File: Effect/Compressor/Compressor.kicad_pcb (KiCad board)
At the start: 2 copper layers, 30 x 62 mm, 40 parts, among them J1 Conn_01x04_Pin, J2 Conn_01x04_Pin, Q1 DMMT5551, Q2 MMBF5103, Q3 DMMT5551, Q4 MMBF5103

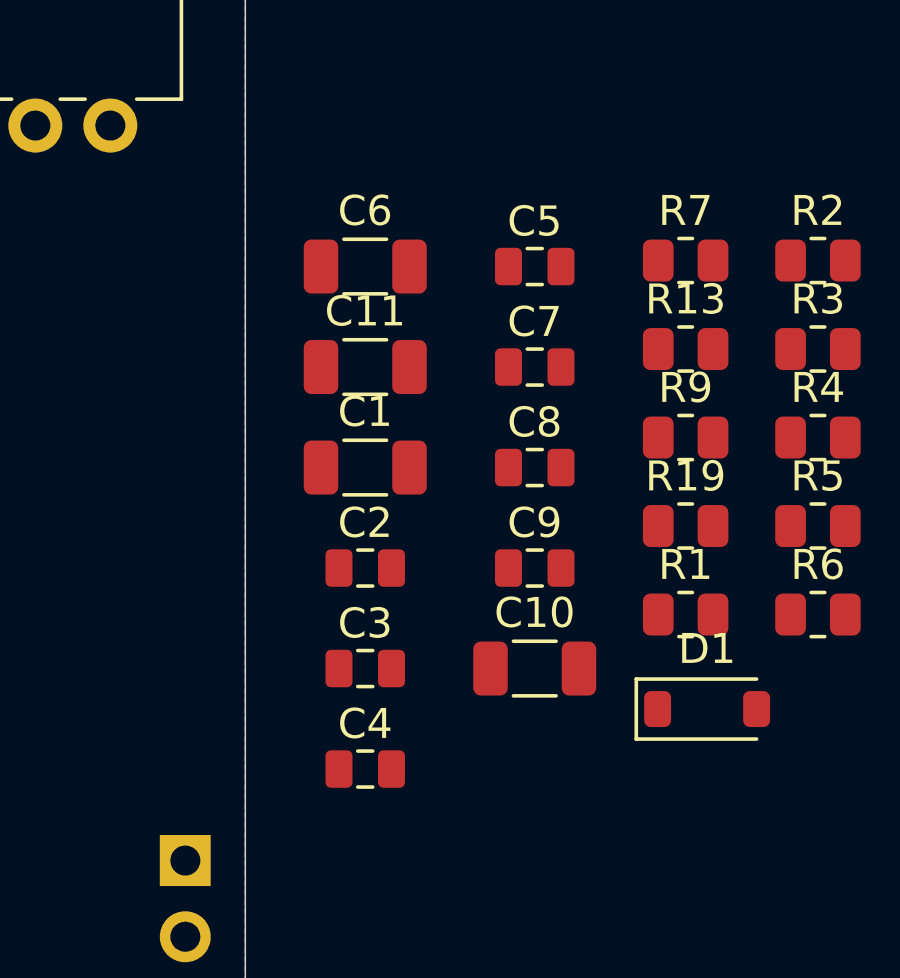
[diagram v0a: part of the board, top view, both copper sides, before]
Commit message: Compressor: Use bigger capacitors in signal path
This just changes the 0.1uF caps in the signal path to 0.47uF ones.
That doesn't fix all ills, but it should pass lower frequency signals a
bit better.

This does make them 1206 footprints, and maybe the board will be a bit
tight.  I'm starting to look at the PCB next.

Signed-off-by: Linus Torvalds <torvalds@linux-foundation.org>
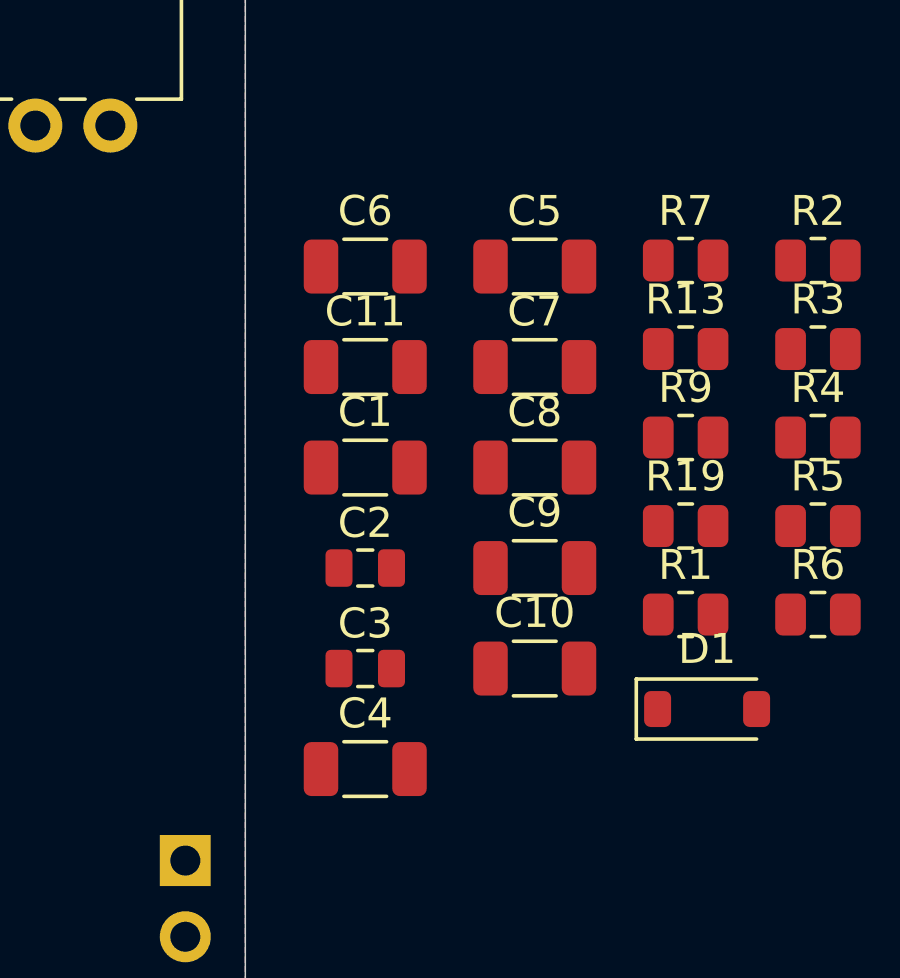
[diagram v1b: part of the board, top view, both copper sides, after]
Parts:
- C4, C5, C7, C8, C9: value 0.1uF -> 0.47uF; footprint Mylib:C_0704_1810Metric -> Capacitor_SMD:C_1206_3216Metric

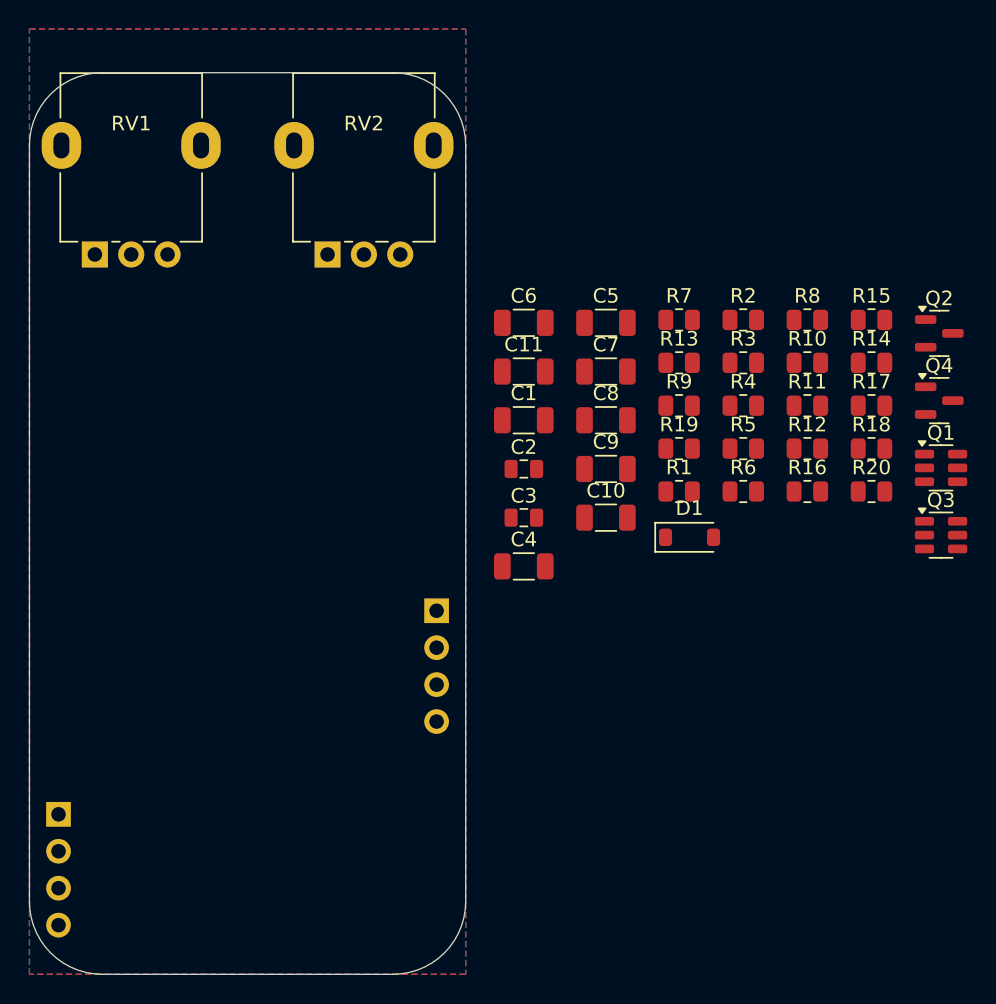
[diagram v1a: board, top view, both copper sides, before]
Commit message: Compressor: do a first PCB layout
I thought this was going to be tighter than it was, so I started laying
out things unnecessarily densely.  Also, the lower left section (the
final signal amplification) would actually have been better off moved up
closer to the volume pot, but by the time I realized that I had tons of
space and shouldn't have squeezed things down there, it was mostly done
and I just didn't bother to change it to make a nicer layout.

I just want to know if this works at all, or if the simulation is just
being unreasonably optimistic.

If it actually works, I'll at a minimum want some kind of "it's now
starting to compress" LED or similar.  And I'd want to do it as a
feedback loop rather than as based purely on input volume (I did
actually simulate a first version of that and it looked doable, but
decided that I really want to get this one done and tested before taking
that step).

Put another way: if this is even remotely usable, I'll make bigger
changes that would result in a complete re-layout anyway, so no point in
worrying over-much about this not being a particularly nice layout.

Signed-off-by: Linus Torvalds <torvalds@linux-foundation.org>
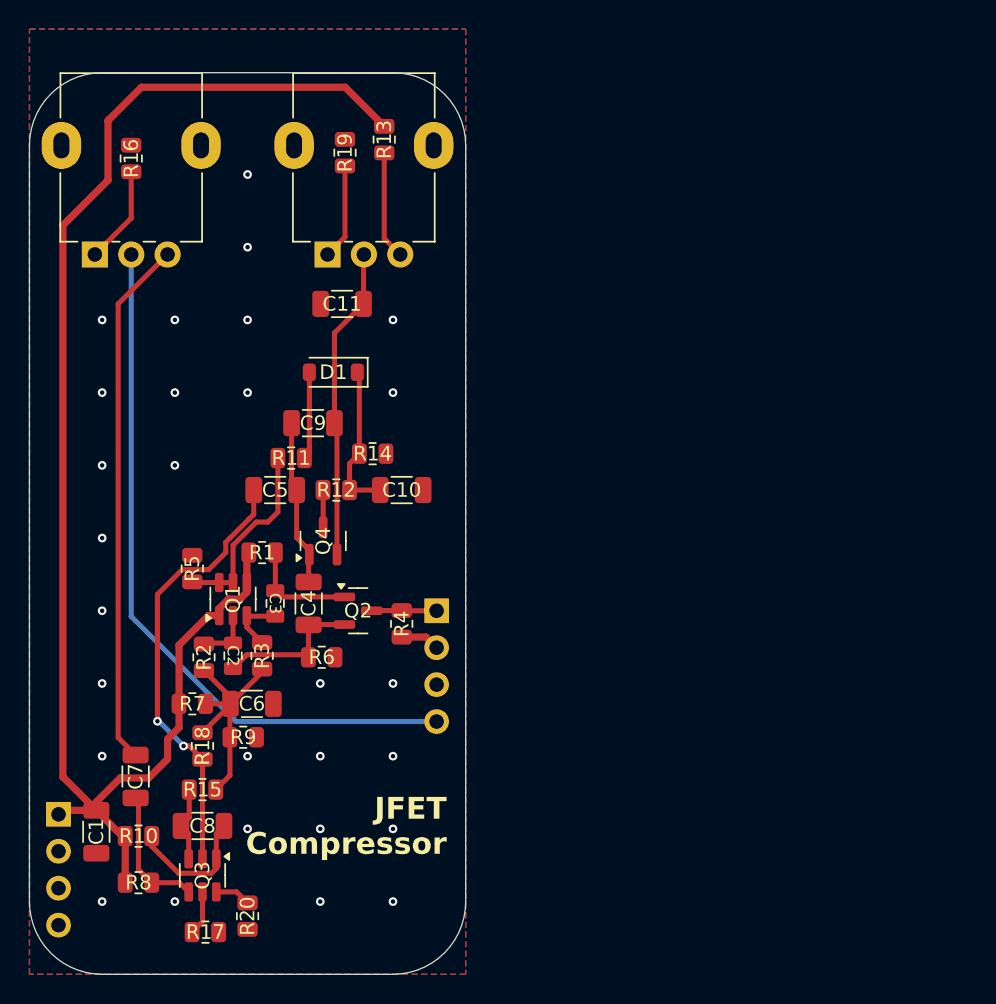
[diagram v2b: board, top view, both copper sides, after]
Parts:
- moved R8 60.1 mm to (92.5, 118.7)
- moved R17 58.4 mm to (97.1, 122.1)
- moved R10 56.3 mm to (92.5, 115.5)
- moved R15 56.2 mm to (96.9, 112.3)
- moved Q3 55.9 mm to (96.9, 118.2), turned to -90 degrees
- moved R20 51.9 mm to (100.0, 121.0), turned to -90 degrees
- moved R16 51.8 mm to (92.0, 68.9), turned to 90 degrees
- moved R18 50.3 mm to (96.9, 109.3), turned to 90 degrees
- moved Q1 49.5 mm to (99.0, 99.2), turned to 90 degrees
- moved Q2 44.3 mm to (107.6, 100.0)
- moved R2 43.7 mm to (97.0, 103.2), turned to -90 degrees
- moved Q4 43.5 mm to (105.2, 95.2), turned to 90 degrees
- moved C7 42.7 mm to (92.3, 111.4), turned to -90 degrees
- moved R7 42.6 mm to (96.2, 106.4)
- moved C1 40.8 mm to (89.6, 115.2), turned to -90 degrees
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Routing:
- net +V: track 0.00 -> 103.5 mm
- net OUT: track 0.00 -> 48.9 mm
- net Net-(C7-Pad1): track 0.00 -> 36.3 mm
- net COMPRESSED: track 0.00 -> 30.7 mm, vias 0 -> 2
- net JFETBIAS: track 0.00 -> 21.5 mm
- net VBIAS: track 0.00 -> 17.1 mm
- net RECT: track 0.00 -> 13.1 mm
- net Net-(Q4-D): track 0.00 -> 11.5 mm
- net Net-(D1-K): track 0.00 -> 10.5 mm
- net BUF: track 0.00 -> 10.4 mm
- net Net-(Q3A-C): track 0.00 -> 9.18 mm
- net Net-(Q3B-C): track 0.00 -> 9.09 mm
- net BUF_NOT: track 0.00 -> 7.57 mm
- net Net-(R13-Pad2): track 0.00 -> 7.44 mm
- net Net-(R16-Pad1): track 0.00 -> 6.72 mm
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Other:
- board text added: "JFET Compressor"

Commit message: Compressor: do PCB layout for the new design
As expected, this was much easier due to the simpler schematic for the
much more straightforward design.

Signed-off-by: Linus Torvalds <torvalds@linux-foundation.org>
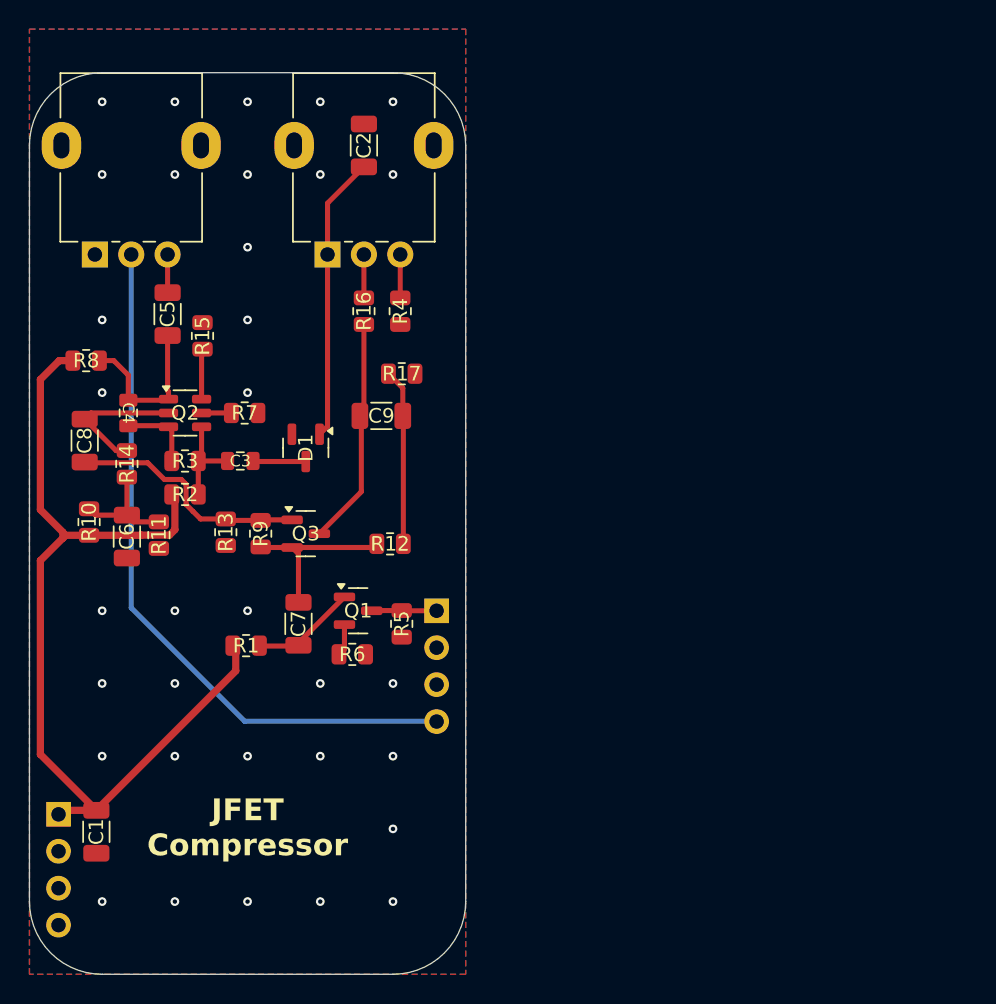
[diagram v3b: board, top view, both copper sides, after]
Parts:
- removed C10: 10uF, Capacitor_SMD:C_1206_3216Metric
- removed C11: 22uF, Capacitor_SMD:C_1206_3216Metric
- removed the Q1 at (99.0, 99.2)
- removed Q4: MMBF5103, Package_TO_SOT_SMD:SOT-23
- removed R18, R19: 100k, Resistor_SMD:R_0805_2012Metric
- removed R20: 3k3, Resistor_SMD:R_0805_2012Metric
- removed the R5 at (96.2, 97.1)
- added Q2: DMMT5551, Package_TO_SOT_SMD:SOT-23-6, F.Cu at (95.7, 86.4)
- added R4: 47k, Resistor_SMD:R_0805_2012Metric, F.Cu at (110.5, 79.4)
- C2: value 0.1uF -> 1uF; footprint Mylib:C_0704_1810Metric -> Capacitor_SMD:C_1206_3216Metric
- C4: value 0.47uF -> 0.1uF; footprint Capacitor_SMD:C_1206_3216Metric -> Mylib:C_0704_1810Metric
- C5, C7, C8: value 0.47uF -> 1uF
- C9: value 0.47uF -> 22nF
- D1: value BAT41Z -> BAT54S-SOT-23-3; footprint Diode_SMD:D_SOD-123 -> Package_TO_SOT_SMD:SOT-23
- Q3: value DMMT5551 -> MMBF5103; footprint Package_TO_SOT_SMD:SOT-23-6 -> Package_TO_SOT_SMD:SOT-23
- R1: value 1k -> 1k5
- R10: value 10k -> 100k
- R11: value 1k -> 33k
- R13: value 160k -> 4k7
- R14: value 1MEG -> 100k
- R15, R7: value 100k -> 3k3
- R16: value 22k -> 1MEG
- R17: value 3k3 -> 100k
- R2: value 100k -> 10k
- R3: value 100k -> 560k
- moved R17 40.7 mm to (110.6, 83.7)
- moved C2 36.2 mm to (108.0, 68.0), turned to 90 degrees
- moved R8 36.1 mm to (88.9, 82.8)
- moved R15 31.2 mm to (96.9, 81.1), turned to 90 degrees
- moved R13 29.1 mm to (98.5, 94.6)
- moved C8 27.7 mm to (88.8, 88.3), turned to 90 degrees
- moved Q3 24.5 mm to (104.0, 94.7), turned to 0 degrees
- moved R10 21.9 mm to (89.1, 93.9), turned to -90 degrees
- moved R7 20.3 mm to (99.8, 86.4)
- moved R16 19.1 mm to (108.0, 79.4), turned to -90 degrees
- moved C4 18.0 mm to (91.8, 86.4)
- moved R14 16.9 mm to (91.7, 89.9), turned to 90 degrees
- moved RV1 16.0 mm to (108.0, 68.0)
- moved RV2 16.0 mm to (92.0, 68.0)
- moved C7 15.4 mm to (103.5, 100.9), turned to 90 degrees
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- renumbered Q2 to Q1, R4 to R5
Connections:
- C2 pad 1: Net-(Q1A-B) -> RECT
- C2 pad 2: BUF -> GND
- C3 pad 1: BUF_NOT -> Net-(Q2B-C)
- C3 pad 2: Net-(Q1B-B) -> Net-(D1-COM)
- C4 pad 1: Net-(Q4-D) -> FB
- C4 pad 2: BUF -> Net-(Q2B-B)
- C5 pad 1: COMPRESSED -> FB
- C5 pad 2: Net-(Q4-D) -> Net-(C5-Pad2)
- C7 pad 1: Net-(C7-Pad1) -> BUF_IN
- C7 pad 2: Net-(Q3B-C) -> Net-(Q3-S)
- C8 pad 1: Net-(Q3B-B) -> Net-(Q3-D)
- C8 pad 2: Net-(Q3A-C) -> Net-(Q2A-B)
- C9 pad 1: Net-(Q4-D) -> Net-(C9-Pad1)
- C9 pad 2: JFETBIAS -> Net-(Q3-G)
- D1 pad 1: Net-(D1-K) -> RECT
- D1 pad 2: Net-(D1-A) -> GND
- Q1 pad 1: BUF_NOT -> BUF_IN
- Q1 pad 2: BUF -> Net-(Q1-S)
- Q3 pad 1: Net-(Q3A-C) -> Net-(Q3-D)
- Q3 pad 2: COMPRESSED -> Net-(Q3-S)
- Q3 pad 3: Net-(Q3B-B) -> Net-(Q3-G)
- R1 pad 2: BUF_NOT -> BUF_IN
- R10 pad 1: +V -> VBIAS
- R10 pad 2: Net-(Q3A-C) -> +V
- R11 pad 1: Net-(D1-A) -> GND
- R11 pad 2: RECT -> VBIAS
- R12 pad 1: CONTROL -> Net-(Q3-S)
- R12 pad 2: Net-(D1-K) -> Net-(C9-Pad1)
- R13 pad 1: +V -> Net-(Q3-D)
- R13 pad 2: Net-(R13-Pad2) -> GND
- R14 pad 1: GND -> VBIAS
- R14 pad 2: Net-(D1-K) -> Net-(Q2A-B)
- R15 pad 1: Net-(Q3B-B) -> Net-(Q2A-E)
- R15 pad 2: VBIAS -> GND
- R16 pad 1: Net-(R16-Pad1) -> CONTROL
- R16 pad 2: GND -> Net-(Q3-G)
- R17 pad 1: Net-(Q3B-E) -> Net-(C9-Pad1)
- R2 pad 1: Net-(Q1A-B) -> +V
- R2 pad 2: VBIAS -> Net-(Q2B-C)
- R3 pad 1: Net-(Q1B-B) -> Net-(Q2B-C)
- R3 pad 2: VBIAS -> Net-(Q2B-B)
- R6 pad 1: BUF -> Net-(Q1-S)
- R7 pad 1: +V -> Net-(Q2B-E)
- R7 pad 2: VBIAS -> GND
- R8 pad 2: Net-(Q3B-C) -> FB
- R9 pad 1: VBIAS -> Net-(Q3-S)
- R9 pad 2: GND -> Net-(Q3-D)
- RV1 pad 1: Net-(R16-Pad1) -> RECT
- RV1 pad 2: OUT -> CONTROL
- RV1 pad 3: Net-(C7-Pad1) -> Net-(R4-Pad2)
- RV2 pad 1: Net-(R19-Pad1) -> GND
- RV2 pad 2: JFETBIAS -> OUT
- RV2 pad 3: Net-(R13-Pad2) -> Net-(C5-Pad2)
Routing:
- net +V: track 103.5 -> 63.8 mm
- net Net-(C7-Pad1): track 36.3 -> 0.00 mm
- net COMPRESSED: track 30.7 -> 0.00 mm, vias 2 -> 0
- net JFETBIAS: track 21.5 -> 0.00 mm
- net Net-(Q3-D): track 0.00 -> 16.8 mm
- net Net-(Q3-G): track 0.00 -> 15.7 mm
- net Net-(C9-Pad1): track 0.00 -> 12.1 mm
- net Net-(Q3-S): track 0.00 -> 12.1 mm
- net Net-(Q4-D): track 11.5 -> 0.00 mm
- net FB: track 0.00 -> 11.3 mm
- net Net-(D1-K): track 10.5 -> 0.00 mm
- net BUF: track 10.4 -> 0.00 mm
- net Net-(Q2A-B): track 0.00 -> 9.73 mm
- net VBIAS: track 17.1 -> 7.79 mm
- net Net-(Q3A-C): track 9.18 -> 0.00 mm
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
